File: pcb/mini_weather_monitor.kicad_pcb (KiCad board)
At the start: 2 copper layers, 135 x 72 mm, 6 parts, among them U1 module_mpu6050, U2 4.0inch_SPI_MSP4021, U2_BME280 module_bme280, U3 neo6mv2, U3_BH1750 module_bh1750

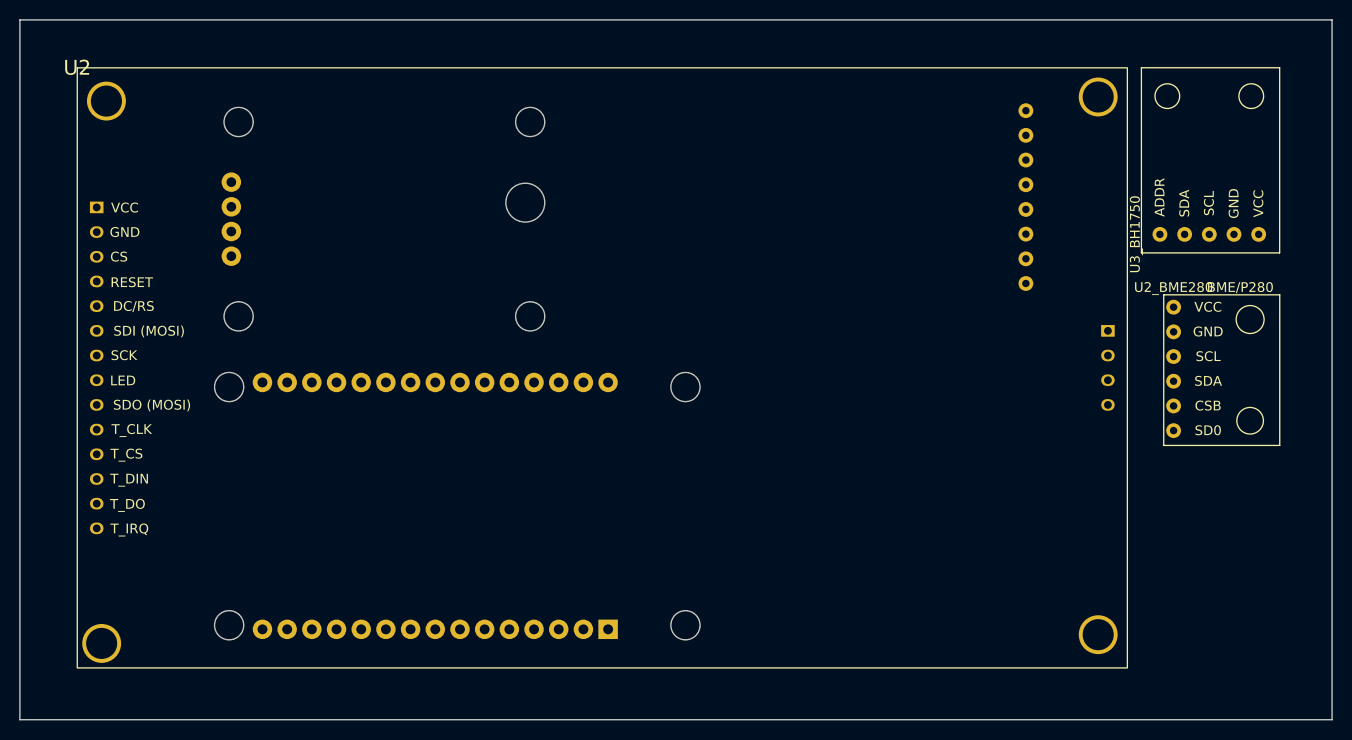
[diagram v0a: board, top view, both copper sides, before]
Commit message: wip, with MPU6050, but will switch to SW520D
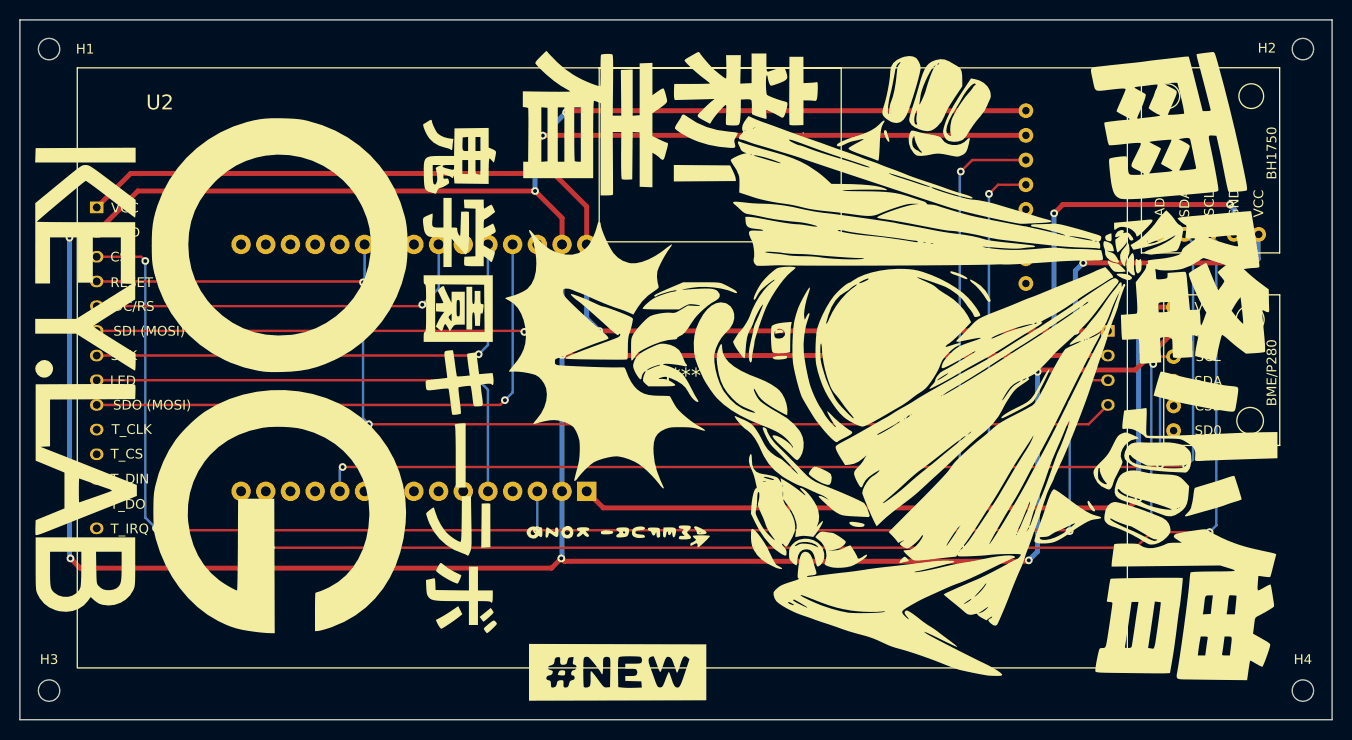
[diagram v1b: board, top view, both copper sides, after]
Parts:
- removed U3: neo6mv2, gps:GY-NEO6MV2
- added G***: LOGO, amefurikozo:amefurikozo_poster, F.Cu at (133.7, 100.6)
- added G***: LOGO, amefurikozo:amefurikozo_poster, B.Cu at (135.3, 98.8)
- added H1: MountingHole, MountingHole:MountingHole_2.2mm_M2, F.Cu at (69.0, 67.0)
- added H2: MountingHole, MountingHole:MountingHole_2.2mm_M2, F.Cu at (198.0, 67.0)
- added H3: MountingHole, MountingHole:MountingHole_2.2mm_M2, F.Cu at (69.0, 133.0)
- added H4: MountingHole, MountingHole:MountingHole_2.2mm_M2, F.Cu at (198.0, 133.0)
- moved U_ESP32_DEVKIT_V1 14.4 mm to (108.8, 99.8)
- renumbered U3_BH1750 to BH1750
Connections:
- U_ESP32_DEVKIT_V1 pad 12: Net-(U3-Pad2) -> unconnected-(U_ESP32_DEVKIT_V1-Pad12)
- U_ESP32_DEVKIT_V1 pad 13: Net-(U3-Pad3) -> unconnected-(U_ESP32_DEVKIT_V1-Pad13)
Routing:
- net GND: track 0.00 -> 407.6 mm, vias 0 -> 11
- net VCC: track 0.00 -> 201.2 mm, vias 0 -> 6
- net Net-(U1-Pad3): track 0.00 -> 200.3 mm, vias 0 -> 6
- net Net-(U1-Pad4): track 0.00 -> 155.6 mm, vias 0 -> 5
- net Net-(U2-Pad3): track 0.00 -> 149.4 mm, vias 0 -> 5
- net Net-(U2-Pad4): track 0.16 -> 123.1 mm, vias 0 -> 2
- net +3V3: track 0.00 -> 80.5 mm, vias 0 -> 2
- net Net-(U2-Pad9): track 0.00 -> 58.6 mm, vias 0 -> 1
- net Net-(U2-Pad6): track 0.00 -> 53.7 mm, vias 0 -> 1
- net Net-(U2-Pad8): track 0.00 -> 51.1 mm, vias 0 -> 1
- net Net-(U2-Pad7): track 0.00 -> 51.0 mm, vias 0 -> 1
- net Net-(U2-Pad5): track 0.00 -> 40.5 mm, vias 0 -> 1
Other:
- board text added: "amefuri kozo v0.2 indoor weather monitor onigakukey.labo @ 2/2022"

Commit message: fixing orientation with new tilt sensor and adding libraries to repo
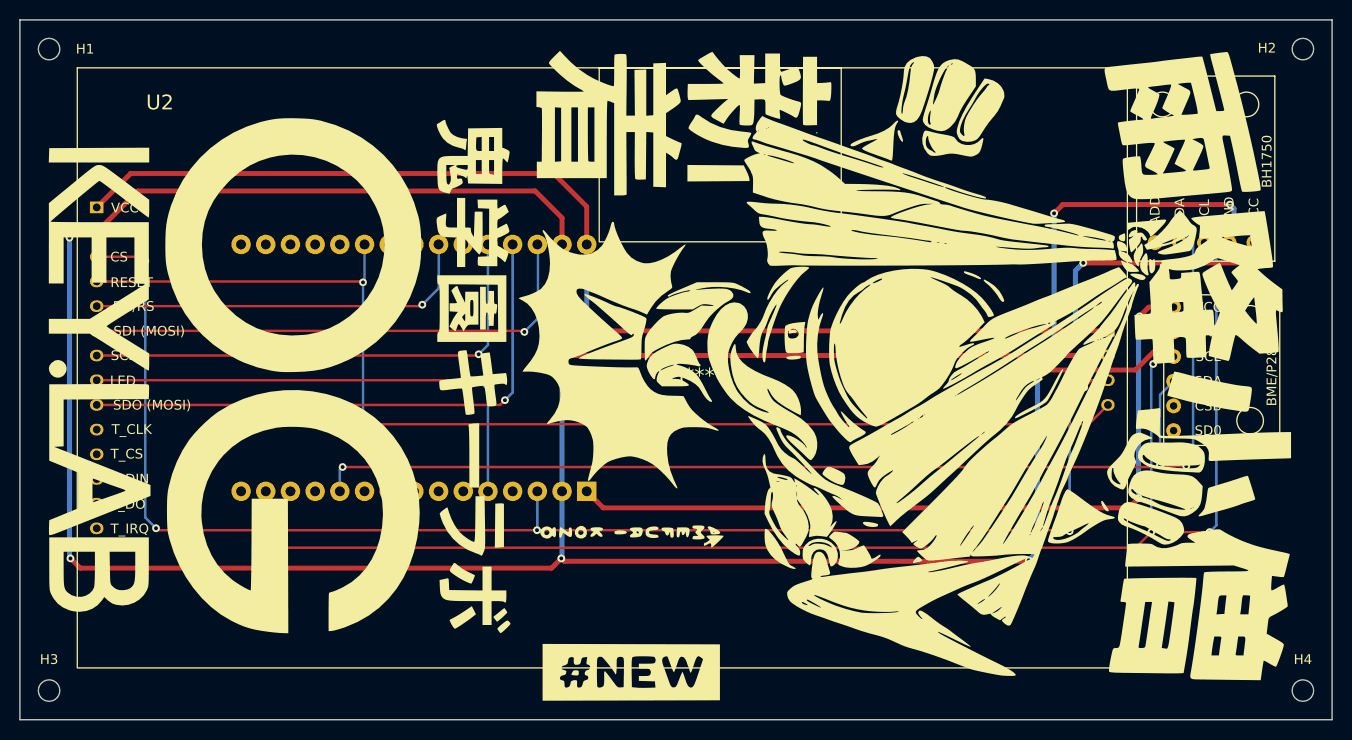
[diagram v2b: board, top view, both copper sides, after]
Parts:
- removed U1: module_mpu6050, usini_sensors:module_mpu6050
- moved G*** 1.48 mm to (136.0, 100.1)
- moved G*** 1.40 mm to (135.1, 100.6)
- moved BH1750 0.99 mm to (193.0, 86.9)
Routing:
- net GND: track 407.6 -> 351.9 mm, vias 11 -> 9
- net VCC: track 201.2 -> 147.0 mm, vias 6 -> 4
- net Net-(U1-Pad3): track 200.3 -> 154.3 mm, vias 6 -> 4
- net Net-(U1-Pad4): track 155.6 -> 123.2 mm, vias 5 -> 3

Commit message: fixxing footprint and pad
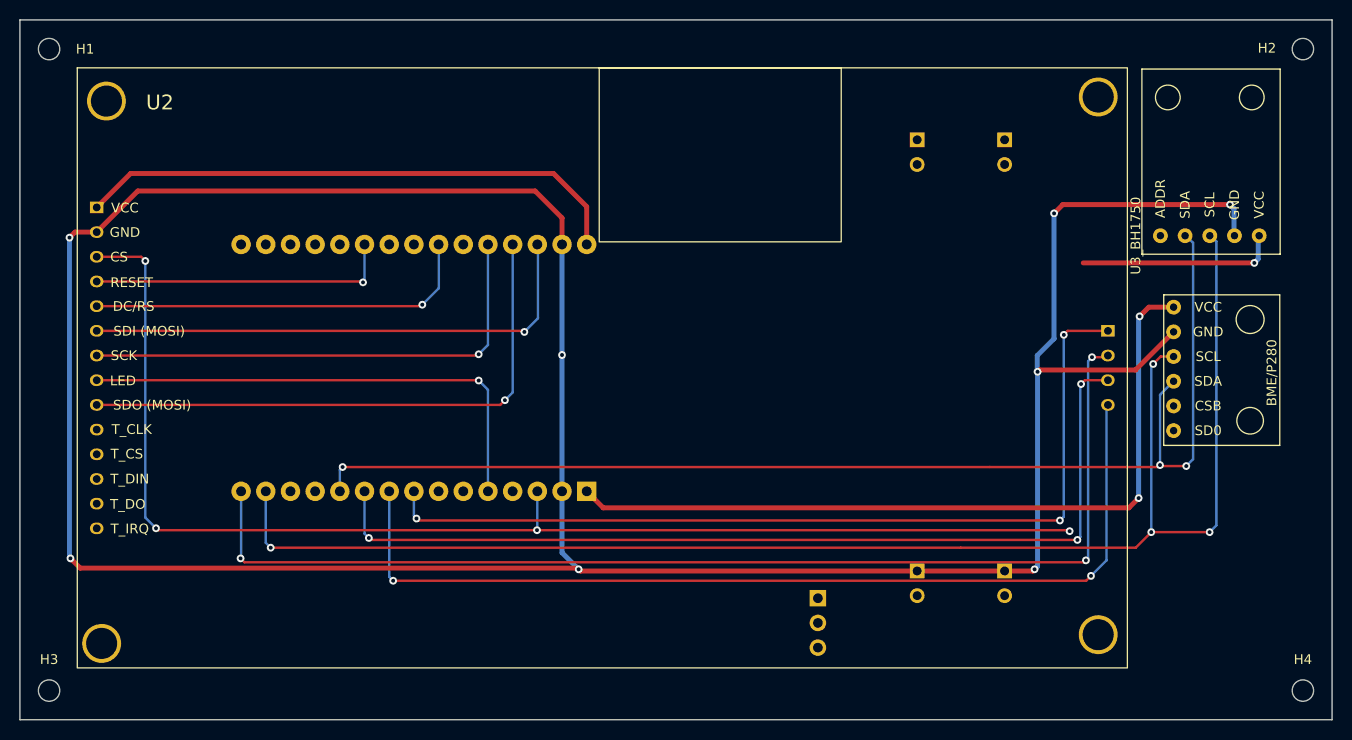
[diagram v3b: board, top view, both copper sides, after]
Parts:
- removed BH1750: module_bh1750, usini_sensors:module_bh1750
- removed G*** (x2): LOGO, amefurikozo:amefurikozo_poster
- added J1: SW-520D, Connector_PinHeader_2.54mm:PinHeader_1x03_P2.54mm_Horizontal, B.Cu at (148.1, 123.5)
- added U1: PowerSupplyMB102_v13, power_supplies:POWERSUPPLYMB102, B.Cu at (154.3, 126.2)
- added U3_BH1750: module_bh1750, usini_sensors:module_bh1750, F.Cu at (193.5, 86.2)
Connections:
- U_ESP32_DEVKIT_V1 pad 4: unconnected-(U_ESP32_DEVKIT_V1-Pad4) -> Net-(J1-Pad1)
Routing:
- net Net-(U2-Pad16): track 0.00 -> 117.3 mm, vias 0 -> 3
- net Net-(U2-Pad18): track 0.00 -> 99.7 mm, vias 0 -> 2
- net Net-(U2-Pad17): track 0.00 -> 97.1 mm, vias 0 -> 3
- net Net-(U2-Pad15): track 0.00 -> 93.2 mm, vias 0 -> 3
- net Net-(U2-Pad4): track 123.1 -> 31.4 mm, vias 2 -> 1
- net VCC: track 147.0 -> 77.9 mm, vias 4 -> 1
- net GND: track 351.9 -> 298.5 mm, vias 9 -> 8
- net Net-(U2-Pad3): track 149.4 -> 131.3 mm, vias 5 -> 4

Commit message: trace cleanup
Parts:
- J1: footprint Connector_PinHeader_2.54mm:PinHeader_1x03_P2.54mm_Horizontal -> tilt:KY020 Tilt
- moved J1 15.1 mm to (135.2, 115.7), turned to -90 degrees
- moved U3_BH1750 0.12 mm to (193.5, 86.1)
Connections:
- U1 pad 4: unconnected-(U1-Pad4) -> GND
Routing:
- net VCC: track 77.9 -> 181.7 mm, vias 1 -> 3
- net +3V3: track 80.5 -> 169.0 mm, vias 2 -> 5
- net Net-(J1-Pad1): track 0.00 -> 46.7 mm, vias 0 -> 1
- net GND: track 298.5 -> 321.8 mm, vias 8 -> 10
- net Net-(U2-Pad18): track 99.7 -> 94.3 mm
- net Net-(U2-Pad16): track 117.3 -> 112.7 mm
- net Net-(U2-Pad15): track 93.2 -> 90.6 mm
- net Net-(U2-Pad17): track 97.1 -> 95.1 mm
- net Net-(U2_BME280-Pad3): track 154.3 -> 152.7 mm
- net Net-(U2-Pad3): track 131.3 -> 129.9 mm
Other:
- board text added: "amefuri kozo v0.5 indoor weather monitor onigakukey.labo @ 6/2022"
- board text removed: "amefuri kozo v0.2 indoor weather monitor onigakukey.labo @ 2/2022"

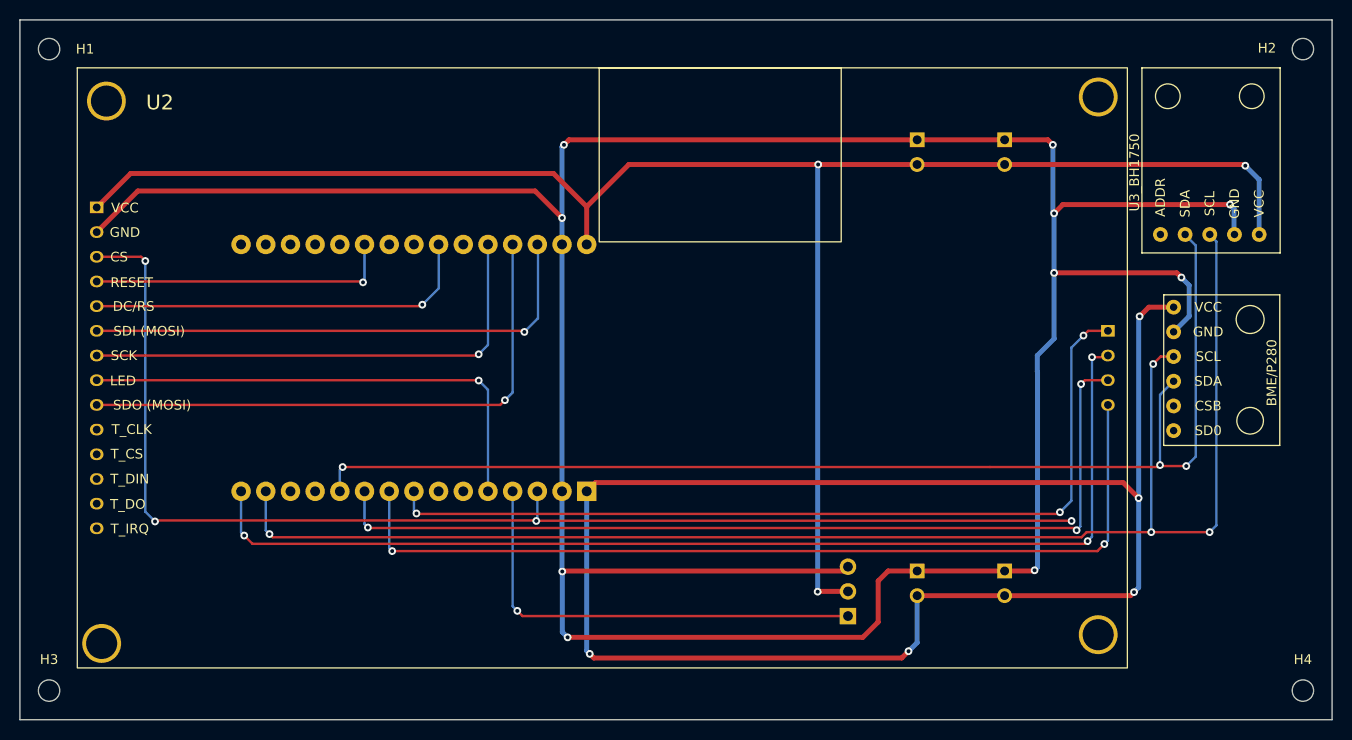
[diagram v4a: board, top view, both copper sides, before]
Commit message: updated silkscreen placement and fixes
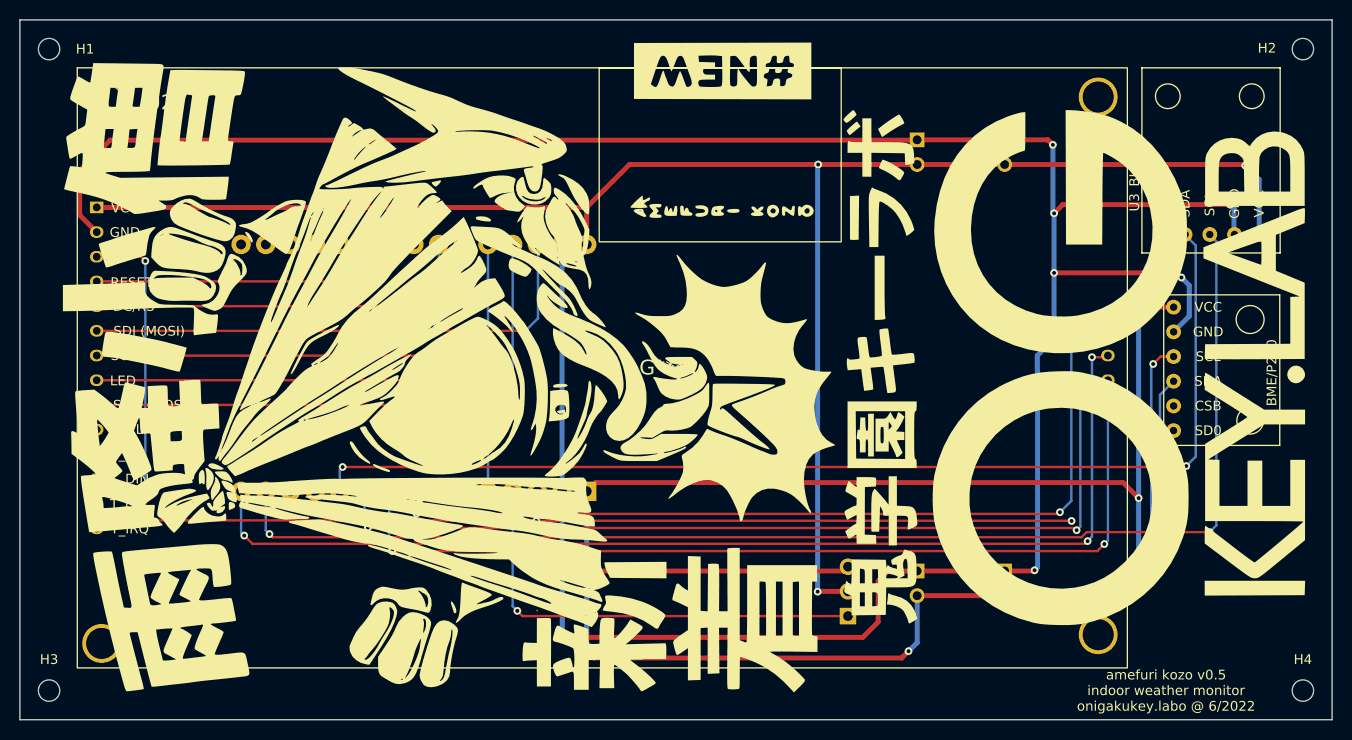
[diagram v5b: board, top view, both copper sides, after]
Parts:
- added G***: LOGO, amefurikozo:amefurikozo_poster, F.Cu at (132.1, 99.8)
- added G***: LOGO, amefurikozo:amefurikozo_poster, B.Cu at (132.0, 99.9)
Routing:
- net GND: track 321.8 -> 318.6 mm, vias 10 -> 8
- net VCC: track 181.7 -> 178.9 mm

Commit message: fixing tilt sensor and power connection was not updated from library
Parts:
- removed the G*** at (132.1, 99.8)
- removed the G*** at (132.0, 99.9)
- added G***: LOGO, amefurikozo:amefurikozo_poster, F.Cu at (131.9, 99.9)
- added G***: LOGO, amefurikozo:amefurikozo_poster, B.Cu at (131.9, 99.8)
- moved J1 18.2 mm to (151.6, 108.0), turned to 180 degrees
- renumbered U1 to Ue
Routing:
- net Net-(U2-Pad3): track 129.9 -> 68.6 mm, vias 4 -> 3
- net Net-(J1-Pad1): track 46.7 -> 37.7 mm
- net GND: track 318.6 -> 316.4 mm
- net VCC: track 178.9 -> 178.4 mm, vias 3 -> 2
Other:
- board text added: "amefuri kozo v0.6 indoor weather monitor onigaku.key.labo @ 6/2022"
- board text removed: "amefuri kozo v0.5 indoor weather monitor onigakukey.labo @ 6/2022"
